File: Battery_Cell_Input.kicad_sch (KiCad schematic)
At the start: 34 parts, among them J801 PT_1000, Q801 NMOS, Q802 NMOS, U801 BQ76920PW

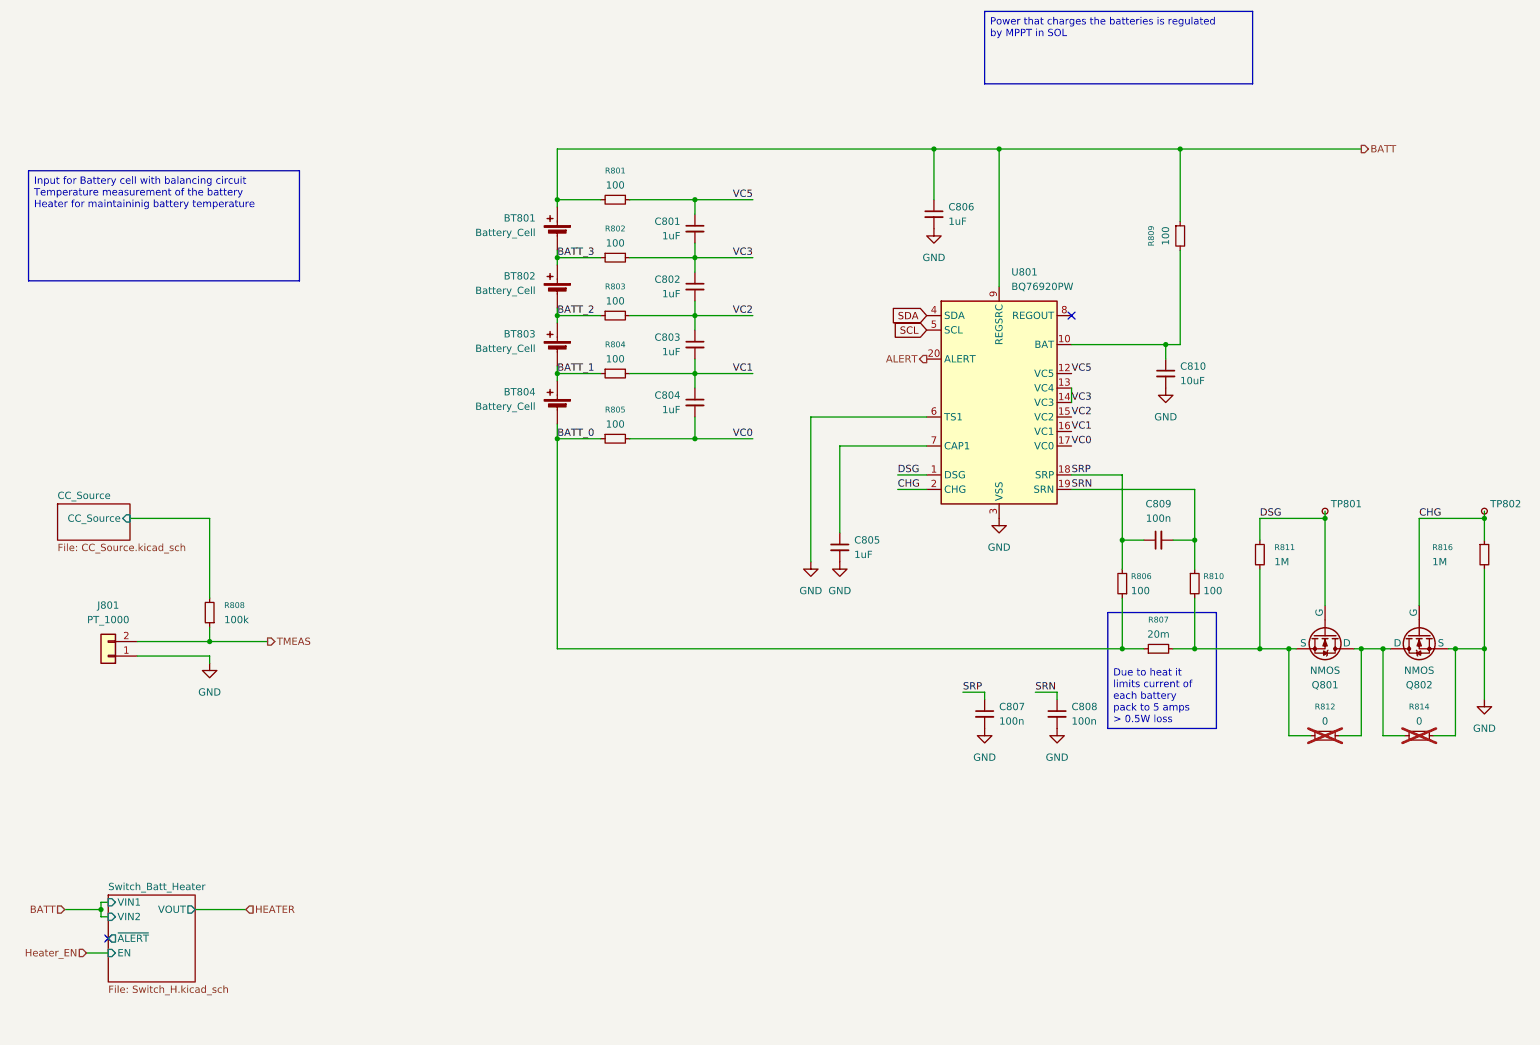
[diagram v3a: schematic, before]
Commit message: restructurization of the entire project improved
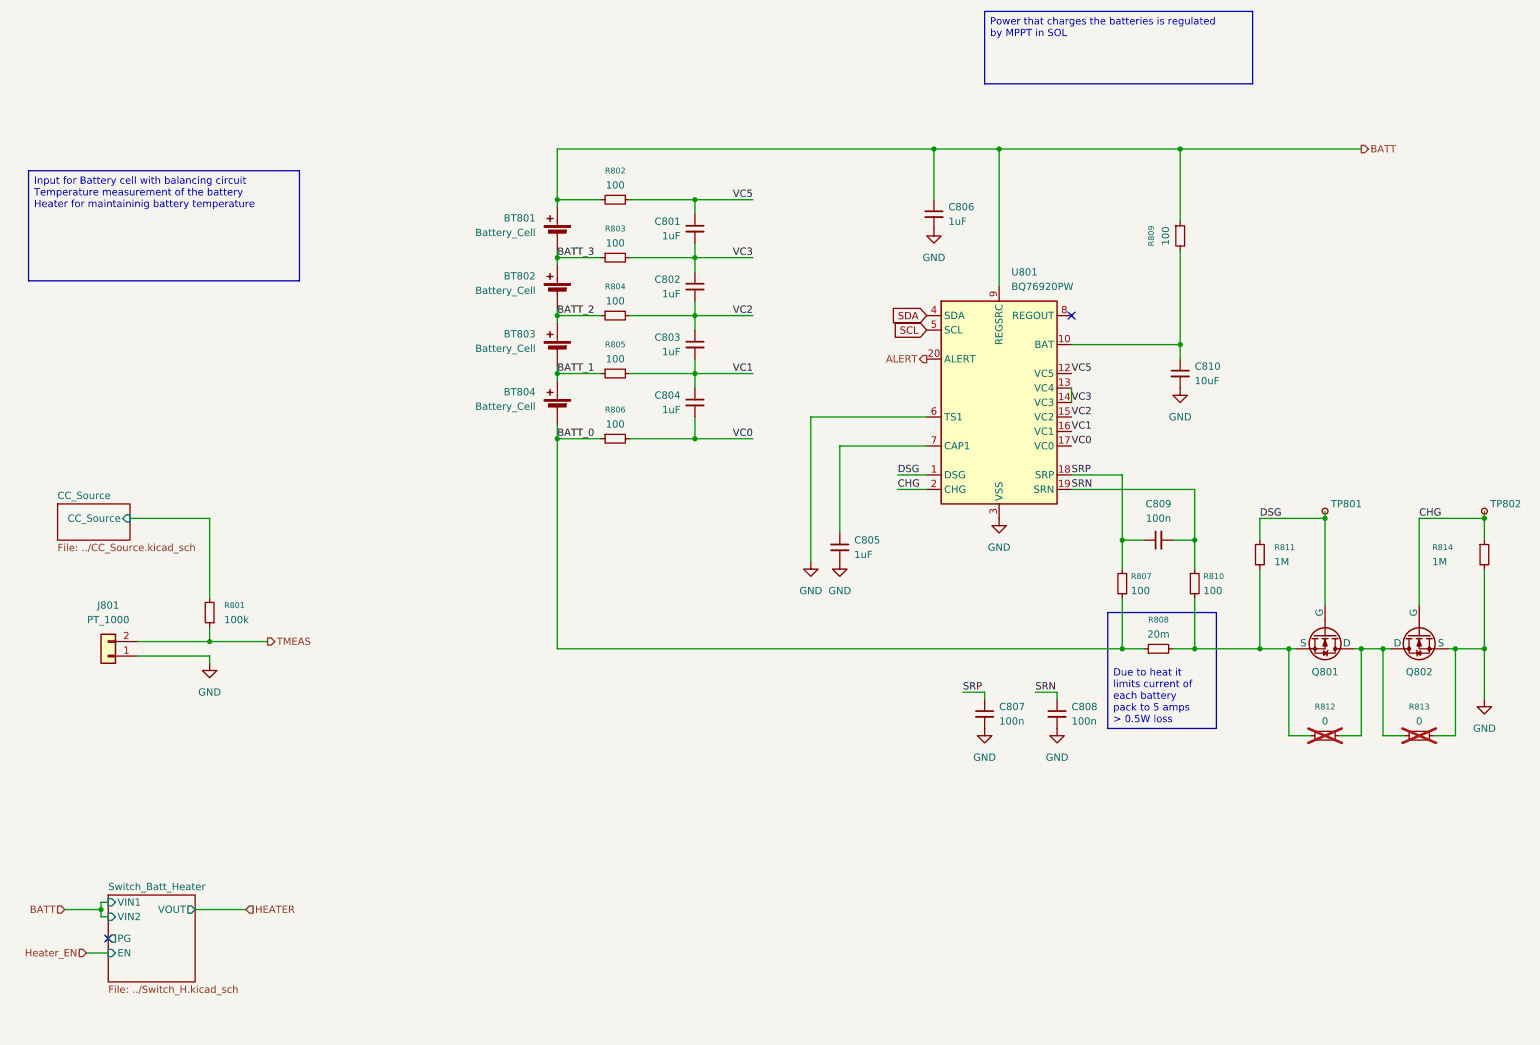
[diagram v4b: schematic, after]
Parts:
- BT801, BT802, BT803, BT804: footprint Outlines:BHC186501P-li-ion -> Connector_PinSocket_2.54mm:PinSocket_1x02_P2.54mm_Vertical
- Q801, Q802: value NMOS -> NVTFWS4D9N04XMTAG
- renumbered R808 to R801, R801 to R802, R802 to R803, R803 to R804, R804 to R805, R805 to R806, R806 to R807, R807 to R808, R814 to R813, R816 to R814
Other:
- sheet CC_Source: file CC_Source.kicad_sch -> ../CC_Source.kicad_sch
- sheet Switch_Batt_Heater: file Switch_H.kicad_sch -> ../Switch_H.kicad_sch
- sheet Switch_Batt_Heater ports: added PG; removed ~{ALERT}
- moved on the sheet: C810
